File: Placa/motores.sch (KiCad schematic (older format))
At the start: 13 parts, among them P3 CONN_5X2

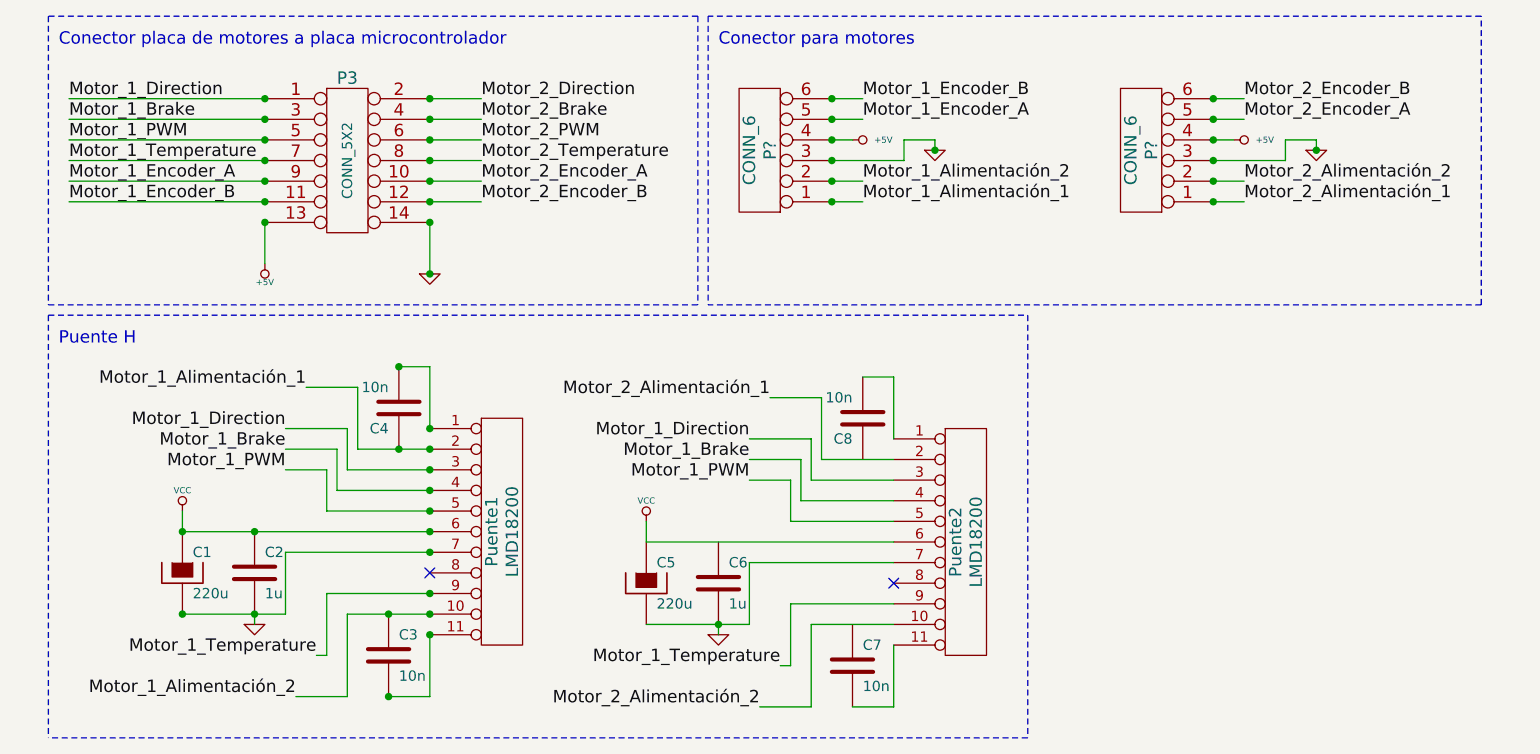
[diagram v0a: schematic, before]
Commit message: Termino PCB motores. Agrego biblioteca LMD18200. Agrego el anteproyecto hecho por Gisela.
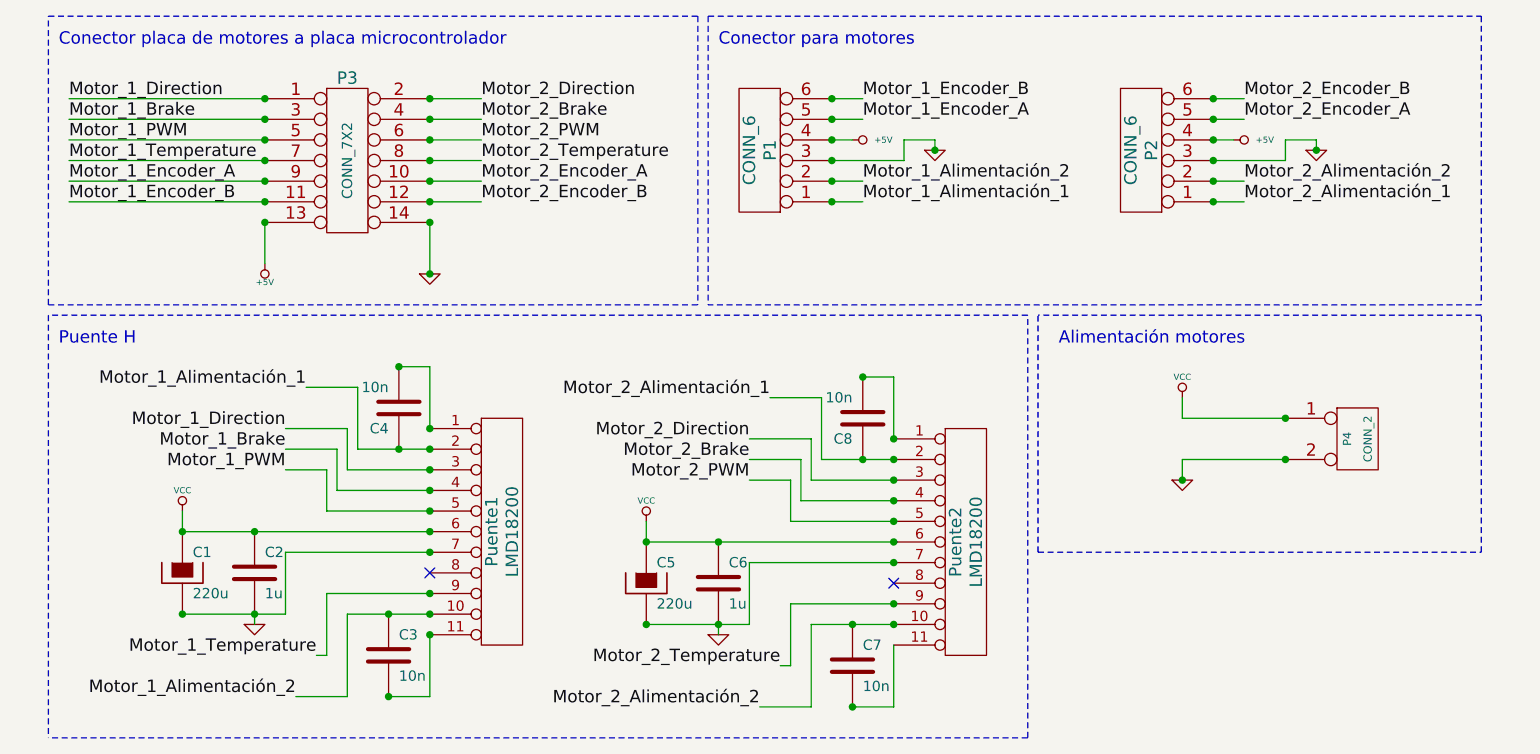
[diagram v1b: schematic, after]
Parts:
- added P4: CONN_2, symbol CONN_2
- P3: value CONN_5X2 -> CONN_7X2
- gave numbers to parts that had none: 2
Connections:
- net GND: now also P4.2 (PM)
- net Motor_1_Brake: no longer Puente2.4 (P4)
- net Motor_1_Direction: no longer Puente2.3 (P3)
- net Motor_1_PWM: no longer Puente2.5 (P5)
- net Motor_1_Temperature: no longer Puente2.9 (P9)
- net Motor_2_Alimentación_1: now also C8.1
- net Motor_2_Alimentación_2: now also C7.1
- net Motor_2_Brake: now also Puente2.4 (P4)
- net Motor_2_Direction: now also Puente2.3 (P3)
- net Motor_2_PWM: now also Puente2.5 (P5)
- net Motor_2_Temperature: now also Puente2.9 (P9)
- net VCC: now also C6.1, P4.1 (P1)
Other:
- note added: "Alimentación motores"

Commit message: Agrego archivos placa potencia. Agrego biblioteca ptn78020w.
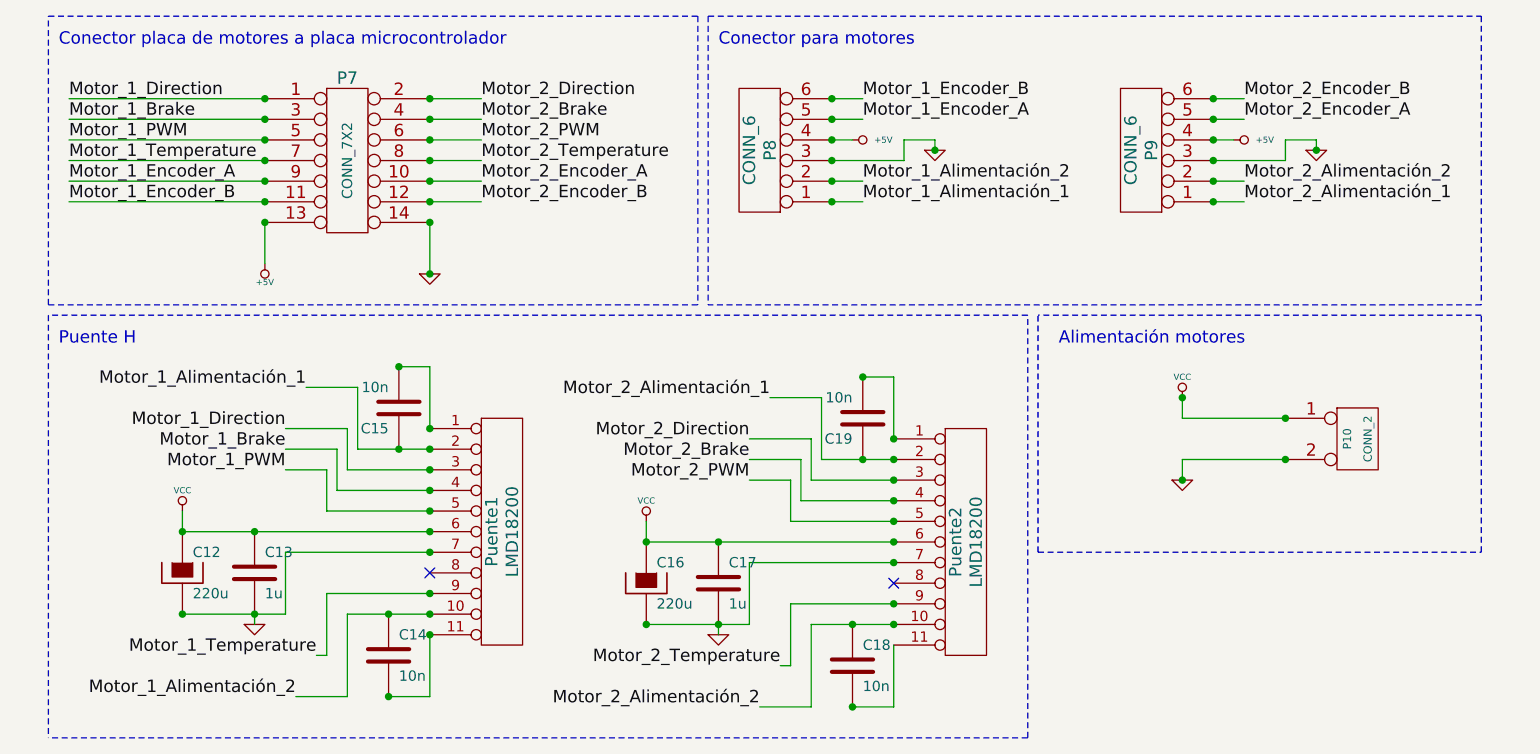
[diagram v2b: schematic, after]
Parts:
- renumbered C1 to C12, C2 to C13, C3 to C14, C4 to C15, C5 to C16, C6 to C17, C7 to C18, C8 to C19, P4 to P10, P3 to P7, P1 to P8, P2 to P9
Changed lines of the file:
@@
-EESchema Schematic File Version 2  date mar 30 abr 2013 20:08:31 ART
+EESchema Schematic File Version 2  date sáb 25 may 2013 16:00:35 ART
 LIBS:power
 LIBS:device
@@
 LIBS:contrib
 LIBS:valves
-LIBS:motores-cache
+LIBS:cny70
+LIBS:L298
+LIBS:ptn4050
+LIBS:ptn78000w
+LIBS:ptn78020w
+LIBS:TCO-cache
 EELAYER 25  0
 EELAYER END
 $Descr A4 11700 8267
 encoding utf-8
-Sheet 1 1
+Sheet 4 5
 Title "TCO - Placa motores"
-Date "30 apr 2013"
+Date "25 may 2013"
 Rev "1"
 Comp ""
@@
 Comment4 ""
 $EndDescr
+Connection ~ 6000 2350
 Connection ~ 6000 2750
 Connection ~ 6500 2450
 Connection ~ 6500 2650
 $Comp
-L GND #PWR01
+L GND #PWR035
 U 1 1 5180451D
 P 6000 2750
-F 0 "#PWR01" H 6000 2750 30  0001 C CNN
+F 0 "#PWR035" H 6000 2750 30  0001 C CNN
 F 1 "GND" H 6000 2680 30  0001 C CNN
 	1    6000 2750
@@
 $EndComp
 $Comp
-L VCC #PWR02
+L VCC #PWR036
 U 1 1 51804519
 P 6000 2350
-F 0 "#PWR02" H 6000 2450 30  0001 C CNN
+F 0 "#PWR036" H 6000 2450 30  0001 C CNN
 F 1 "VCC" H 6000 2450 30  0000 C CNN
 	1    6000 2350
@@
 	6000 2450 6000 2350
 $Comp
-L CONN_2 P4
+L CONN_2 P10
 U 1 1 5180450D
 P 6850 2550
-F 0 "P4" V 6800 2550 40  0000 C CNN
+F 0 "P10" V 6800 2550 40  0000 C CNN
 F 1 "CONN_2" V 6900 2550 40  0000 C CNN
 	1    6850 2550
@@
 Puente H
 $Comp
-L CONN_6 P2
+L CONN_6 P9
 U 1 1 517D87F6
 P 5800 1150
-F 0 "P2" V 5750 1150 60  0000 C CNN
+F 0 "P9" V 5750 1150 60  0000 C CNN
 F 1 "CONN_6" V 5850 1150 60  0000 C CNN
 	1    5800 1150
@@
 Motor_2_Alimentación_2
 $Comp
-L +5V #PWR03
+L +5V #PWR037
 U 1 1 517D87F5
 P 6250 1100
-F 0 "#PWR03" H 6250 1190 20  0001 C CNN
+F 0 "#PWR037" H 6250 1190 20  0001 C CNN
 F 1 "+5V" V 6250 1250 30  0000 C CNN
 	1    6250 1100
@@
 $EndComp
 $Comp
-L GND #PWR04
+L GND #PWR038
 U 1 1 517D87F4
 P 6650 1150
-F 0 "#PWR04" H 6650 1150 30  0001 C CNN
+F 0 "#PWR038" H 6650 1150 30  0001 C CNN
 F 1 "GND" H 6650 1080 30  0001 C CNN
 	1    6650 1150
@@
 Motor_1_Encoder_A
 $Comp
-L GND #PWR05
+L GND #PWR039
 U 1 1 517D878E
 P 4800 1150
-F 0 "#PWR05" H 4800 1150 30  0001 C CNN
+F 0 "#PWR039" H 4800 1150 30  0001 C CNN
 F 1 "GND" H 4800 1080 30  0001 C CNN
 	1    4800 1150
@@
 $EndComp
 $Comp
-L +5V #PWR06
+L +5V #PWR040
 U 1 1 517D877F
 P 4400 1100
-F 0 "#PWR06" H 4400 1190 20  0001 C CNN
+F 0 "#PWR040" H 4400 1190 20  0001 C CNN
 F 1 "+5V" V 4400 1250 30  0000 C CNN
 	1    4400 1100
@@
 Motor_1_Alimentación_1
 $Comp
-L CONN_6 P1
+L CONN_6 P8
 U 1 1 517D8704
 P 3950 1150
-F 0 "P1" V 3900 1150 60  0000 C CNN
+F 0 "P8" V 3900 1150 60  0000 C CNN
 F 1 "CONN_6" V 4000 1150 60  0000 C CNN
 	1    3950 1150
@@
 Motor_2_Direction
 $Comp
-L C C7
+L C C18
 U 1 1 51769D40
 P 4400 3650
-F 0 "C7" H 4450 3750 50  0000 L CNN
+F 0 "C18" H 4450 3750 50  0000 L CNN
 F 1 "10n" H 4450 3550 50  0000 L CNN
 	1    4400 3650
@@
 NoConn ~ 4600 3250
 $Comp
-L GND #PWR07
+L GND #PWR041
 U 1 1 51769D3F
 P 3750 3500
-F 0 "#PWR07" H 3750 3500 30  0001 C CNN
+F 0 "#PWR041" H 3750 3500 30  0001 C CNN
 F 1 "GND" H 3750 3430 30  0001 C CNN
 	1    3750 3500
@@
 $EndComp
 $Comp
-L C C6
+L C C17
 U 1 1 51769D3E
 P 3750 3250
-F 0 "C6" H 3800 3350 50  0000 L CNN
+F 0 "C17" H 3800 3350 50  0000 L CNN
 F 1 "1u" H 3800 3150 50  0000 L CNN
 	1    3750 3250
@@
 $EndComp
 $Comp
-L CAPAPOL C5
+L CAPAPOL C16
 U 1 1 51769D3D
 P 3400 3250
-F 0 "C5" H 3450 3350 50  0000 L CNN
+F 0 "C16" H 3450 3350 50  0000 L CNN
 F 1 "220u" H 3450 3150 50  0000 L CNN
 	1    3400 3250
@@
 $EndComp
 $Comp
-L VCC #PWR08
+L VCC #PWR042
 U 1 1 51769D3C
 P 3400 2950
-F 0 "#PWR08" H 3400 3050 30  0001 C CNN
+F 0 "#PWR042" H 3400 3050 30  0001 C CNN
 F 1 "VCC" H 3400 3050 30  0000 C CNN
 	1    3400 2950
@@
 $EndComp
 $Comp
-L C C8
+L C C19
 U 1 1 51769D3B
 P 4450 2450
-F 0 "C8" H 4500 2550 50  0000 L CNN
+F 0 "C19" H 4500 2550 50  0000 L CNN
 F 1 "10n" H 4500 2350 50  0000 L CNN
 	1    4450 2450
@@
 Motor_1_Direction
 $Comp
-L GND #PWR09
+L GND #PWR043
 U 1 1 51755C0C
 P 2350 1750
-F 0 "#PWR09" H 2350 1750 30  0001 C CNN
+F 0 "#PWR043" H 2350 1750 30  0001 C CNN
 F 1 "GND" H 2350 1680 30  0001 C CNN
 	1    2350 1750
@@
 $EndComp
 $Comp
-L +5V #PWR010
+L +5V #PWR044
 U 1 1 51755BFF
 P 1550 1700
-F 0 "#PWR010" H 1550 1790 20  0001 C CNN
+F 0 "#PWR044" H 1550 1790 20  0001 C CNN
 F 1 "+5V" H 1550 1790 30  0000 C CNN
 	1    1550 1700
@@
 Motor_1_Direction
 $Comp
-L CONN_7X2 P3
+L CONN_7X2 P7
 U 1 1 517556DB
 P 1950 1200
-F 0 "P3" H 1950 1600 60  0000 C CNN
+F 0 "P7" H 1950 1600 60  0000 C CNN
 F 1 "CONN_7X2" V 1950 1200 50  0000 C CNN
 	1    1950 1200
@@
 $EndComp
 $Comp
-L C C3
+L C C14
 U 1 1 51755634
 P 2150 3600
-F 0 "C3" H 2200 3700 50  0000 L CNN
+F 0 "C14" H 2200 3700 50  0000 L CNN
 F 1 "10n" H 2200 3500 50  0000 L CNN
 	1    2150 3600
@@
 NoConn ~ 2350 3200
 $Comp
-L GND #PWR011
+L GND #PWR045
 U 1 1 5175560C
 P 1500 3450
-F 0 "#PWR011" H 1500 3450 30  0001 C CNN
+F 0 "#PWR045" H 1500 3450 30  0001 C CNN
 F 1 "GND" H 1500 3380 30  0001 C CNN
 	1    1500 3450
@@
 $EndComp
 $Comp
-L C C2
+L C C13
 U 1 1 517555EE
 P 1500 3200
-F 0 "C2" H 1550 3300 50  0000 L CNN
+F 0 "C13" H 1550 3300 50  0000 L CNN
 F 1 "1u" H 1550 3100 50  0000 L CNN
 	1    1500 3200
@@
 $EndComp
 $Comp
-L CAPAPOL C1
+L CAPAPOL C12
 U 1 1 517555DF
 P 1150 3200
-F 0 "C1" H 1200 3300 50  0000 L CNN
+F 0 "C12" H 1200 3300 50  0000 L CNN
 F 1 "220u" H 1200 3100 50  0000 L CNN
 	1    1150 3200
@@
 $EndComp
 $Comp
-L VCC #PWR012
+L VCC #PWR046
 U 1 1 517555C8
 P 1150 2900
-F 0 "#PWR012" H 1150 3000 30  0001 C CNN
+F 0 "#PWR046" H 1150 3000 30  0001 C CNN
 F 1 "VCC" H 1150 3000 30  0000 C CNN
 	1    1150 2900
@@
 $EndComp
 $Comp
-L C C4
+L C C15
 U 1 1 5175549B
 P 2200 2400
-F 0 "C4" H 2250 2500 50  0000 L CNN
+F 0 "C15" H 2250 2500 50  0000 L CNN
 F 1 "10n" H 2250 2300 50  0000 L CNN
 	1    2200 2400

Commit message: Agrego retoques en 2da revisión PCB micro
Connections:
- net labels added: +12V
- net labels removed: VCC
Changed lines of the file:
@@
-EESchema Schematic File Version 2  date mar 11 jun 2013 16:06:38 ART
+EESchema Schematic File Version 2  date mar 11 jun 2013 16:28:51 ART
 LIBS:power
 LIBS:device
@@
 Comment4 ""
 $EndDescr
+$Comp
+L +12V #PWR032
+U 1 1 51B77652
+P 1150 2900
+F 0 "#PWR032" H 1150 2850 20  0001 C CNN
+F 1 "+12V" H 1150 3000 30  0000 C CNN
+	1    1150 2900
+	1    0    0    -1
+$EndComp
+$Comp
+L +12V #PWR033
+U 1 1 51B7764D
+P 3400 2950
+F 0 "#PWR033" H 3400 2900 20  0001 C CNN
+F 1 "+12V" H 3400 3050 30  0000 C CNN
+	1    3400 2950
+	1    0    0    -1
+$EndComp
+$Comp
+L +12V #PWR034
+U 1 1 51B77648
+P 6000 2350
+F 0 "#PWR034" H 6000 2300 20  0001 C CNN
+F 1 "+12V" H 6000 2450 30  0000 C CNN
+	1    6000 2350
+	1    0    0    -1
+$EndComp
 Connection ~ 6000 2350
 Connection ~ 6000 2750
@@
 Connection ~ 6500 2650
 $Comp
-L GND #PWR44
+L GND #PWR035
 U 1 1 5180451D
 P 6000 2750
-F 0 "#PWR44" H 6000 2750 30  0001 C CNN
+F 0 "#PWR035" H 6000 2750 30  0001 C CNN
 F 1 "GND" H 6000 2680 30  0001 C CNN
 	1    6000 2750
-	1    0    0    -1
-$EndComp
-$Comp
-L VCC #PWR43
-U 1 1 51804519
-P 6000 2350
-F 0 "#PWR43" H 6000 2450 30  0001 C CNN
-F 1 "VCC" H 6000 2450 30  0000 C CNN
-	1    6000 2350
 	1    0    0    -1
 $EndComp
@@
 Motor_2_Alimentación_2
 $Comp
-L +5V #PWR45
+L +5V #PWR036
 U 1 1 517D87F5
 P 6250 1100
-F 0 "#PWR45" H 6250 1190 20  0001 C CNN
+F 0 "#PWR036" H 6250 1190 20  0001 C CNN
 F 1 "+5V" V 6250 1250 30  0000 C CNN
 	1    6250 1100
@@
 $EndComp
 $Comp
-L GND #PWR46
+L GND #PWR037
 U 1 1 517D87F4
 P 6650 1150
-F 0 "#PWR46" H 6650 1150 30  0001 C CNN
+F 0 "#PWR037" H 6650 1150 30  0001 C CNN
 F 1 "GND" H 6650 1080 30  0001 C CNN
 	1    6650 1150
@@
 Motor_1_Encoder_A
 $Comp
-L GND #PWR42
+L GND #PWR038
 U 1 1 517D878E
 P 4800 1150
-F 0 "#PWR42" H 4800 1150 30  0001 C CNN
+F 0 "#PWR038" H 4800 1150 30  0001 C CNN
 F 1 "GND" H 4800 1080 30  0001 C CNN
 	1    4800 1150
@@
 $EndComp
 $Comp
-L +5V #PWR41
+L +5V #PWR039
 U 1 1 517D877F
 P 4400 1100
-F 0 "#PWR41" H 4400 1190 20  0001 C CNN
+F 0 "#PWR039" H 4400 1190 20  0001 C CNN
 F 1 "+5V" V 4400 1250 30  0000 C CNN
 	1    4400 1100
@@
 NoConn ~ 4600 3250
 $Comp
-L GND #PWR40
+L GND #PWR040
 U 1 1 51769D3F
 P 3750 3500
-F 0 "#PWR40" H 3750 3500 30  0001 C CNN
+F 0 "#PWR040" H 3750 3500 30  0001 C CNN
 F 1 "GND" H 3750 3430 30  0001 C CNN
 	1    3750 3500
@@
 F 1 "220u" H 3450 3150 50  0000 L CNN
 	1    3400 3250
-	1    0    0    -1
-$EndComp
-$Comp
-L VCC #PWR39
-U 1 1 51769D3C
-P 3400 2950
-F 0 "#PWR39" H 3400 3050 30  0001 C CNN
-F 1 "VCC" H 3400 3050 30  0000 C CNN
-	1    3400 2950
 	1    0    0    -1
 $EndComp
@@
 Motor_1_Direction
 $Comp
-L GND #PWR38
+L GND #PWR041
 U 1 1 51755C0C
 P 2350 1750
-F 0 "#PWR38" H 2350 1750 30  0001 C CNN
+F 0 "#PWR041" H 2350 1750 30  0001 C CNN
 F 1 "GND" H 2350 1680 30  0001 C CNN
 	1    2350 1750
@@
 $EndComp
 $Comp
-L +5V #PWR37
+L +5V #PWR042
 U 1 1 51755BFF
 P 1550 1700
-F 0 "#PWR37" H 1550 1790 20  0001 C CNN
+F 0 "#PWR042" H 1550 1790 20  0001 C CNN
 F 1 "+5V" H 1550 1790 30  0000 C CNN
 	1    1550 1700
@@
 NoConn ~ 2350 3200
 $Comp
-L GND #PWR36
+L GND #PWR043
 U 1 1 5175560C
 P 1500 3450
-F 0 "#PWR36" H 1500 3450 30  0001 C CNN
+F 0 "#PWR043" H 1500 3450 30  0001 C CNN
 F 1 "GND" H 1500 3380 30  0001 C CNN
 	1    1500 3450
@@
 	1    0    0    -1
 $EndComp
-$Comp
-L VCC #PWR35
-U 1 1 517555C8
-P 1150 2900
-F 0 "#PWR35" H 1150 3000 30  0001 C CNN
-F 1 "VCC" H 1150 3000 30  0000 C CNN
-	1    1150 2900
-	1    0    0    -1
-$EndComp

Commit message: Agrego medición del piso, pero no funciona. Seguramente olvidé alguna configuración.
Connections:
- net labels added: VCC
- net labels removed: +12V
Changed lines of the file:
@@
-EESchema Schematic File Version 2  date mar 11 jun 2013 16:28:51 ART
+EESchema Schematic File Version 2  date jue 06 jun 2013 20:07:57 ART
 LIBS:power
 LIBS:device
@@
 LIBS:ptn78000w
 LIBS:ptn78020w
-LIBS:TCO-cache
 EELAYER 25  0
 EELAYER END
@@
 Sheet 4 5
 Title "TCO - Placa motores"
-Date "11 jun 2013"
-Rev "2"
+Date "6 jun 2013"
+Rev "1"
 Comp ""
 Comment1 ""
@@
 Comment4 ""
 $EndDescr
-$Comp
-L +12V #PWR032
-U 1 1 51B77652
-P 1150 2900
-F 0 "#PWR032" H 1150 2850 20  0001 C CNN
-F 1 "+12V" H 1150 3000 30  0000 C CNN
-	1    1150 2900
-	1    0    0    -1
-$EndComp
-$Comp
-L +12V #PWR033
-U 1 1 51B7764D
-P 3400 2950
-F 0 "#PWR033" H 3400 2900 20  0001 C CNN
-F 1 "+12V" H 3400 3050 30  0000 C CNN
-	1    3400 2950
-	1    0    0    -1
-$EndComp
-$Comp
-L +12V #PWR034
-U 1 1 51B77648
-P 6000 2350
-F 0 "#PWR034" H 6000 2300 20  0001 C CNN
-F 1 "+12V" H 6000 2450 30  0000 C CNN
-	1    6000 2350
-	1    0    0    -1
-$EndComp
 Connection ~ 6000 2350
 Connection ~ 6000 2750
@@
 Connection ~ 6500 2650
 $Comp
-L GND #PWR035
+L GND #PWR44
 U 1 1 5180451D
 P 6000 2750
-F 0 "#PWR035" H 6000 2750 30  0001 C CNN
+F 0 "#PWR44" H 6000 2750 30  0001 C CNN
 F 1 "GND" H 6000 2680 30  0001 C CNN
 	1    6000 2750
+	1    0    0    -1
+$EndComp
+$Comp
+L VCC #PWR43
+U 1 1 51804519
+P 6000 2350
+F 0 "#PWR43" H 6000 2450 30  0001 C CNN
+F 1 "VCC" H 6000 2450 30  0000 C CNN
+	1    6000 2350
 	1    0    0    -1
 $EndComp
@@
 Motor_2_Alimentación_2
 $Comp
-L +5V #PWR036
+L +5V #PWR45
 U 1 1 517D87F5
 P 6250 1100
-F 0 "#PWR036" H 6250 1190 20  0001 C CNN
+F 0 "#PWR45" H 6250 1190 20  0001 C CNN
 F 1 "+5V" V 6250 1250 30  0000 C CNN
 	1    6250 1100
@@
 $EndComp
 $Comp
-L GND #PWR037
+L GND #PWR46
 U 1 1 517D87F4
 P 6650 1150
-F 0 "#PWR037" H 6650 1150 30  0001 C CNN
+F 0 "#PWR46" H 6650 1150 30  0001 C CNN
 F 1 "GND" H 6650 1080 30  0001 C CNN
 	1    6650 1150
@@
 Motor_1_Encoder_A
 $Comp
-L GND #PWR038
+L GND #PWR42
 U 1 1 517D878E
 P 4800 1150
-F 0 "#PWR038" H 4800 1150 30  0001 C CNN
+F 0 "#PWR42" H 4800 1150 30  0001 C CNN
 F 1 "GND" H 4800 1080 30  0001 C CNN
 	1    4800 1150
@@
 $EndComp
 $Comp
-L +5V #PWR039
+L +5V #PWR41
 U 1 1 517D877F
 P 4400 1100
-F 0 "#PWR039" H 4400 1190 20  0001 C CNN
+F 0 "#PWR41" H 4400 1190 20  0001 C CNN
 F 1 "+5V" V 4400 1250 30  0000 C CNN
 	1    4400 1100
@@
 NoConn ~ 4600 3250
 $Comp
-L GND #PWR040
+L GND #PWR40
 U 1 1 51769D3F
 P 3750 3500
-F 0 "#PWR040" H 3750 3500 30  0001 C CNN
+F 0 "#PWR40" H 3750 3500 30  0001 C CNN
 F 1 "GND" H 3750 3430 30  0001 C CNN
 	1    3750 3500
@@
 F 1 "220u" H 3450 3150 50  0000 L CNN
 	1    3400 3250
+	1    0    0    -1
+$EndComp
+$Comp
+L VCC #PWR39
+U 1 1 51769D3C
+P 3400 2950
+F 0 "#PWR39" H 3400 3050 30  0001 C CNN
+F 1 "VCC" H 3400 3050 30  0000 C CNN
+	1    3400 2950
 	1    0    0    -1
 $EndComp
@@
 Motor_1_Direction
 $Comp
-L GND #PWR041
+L GND #PWR38
 U 1 1 51755C0C
 P 2350 1750
-F 0 "#PWR041" H 2350 1750 30  0001 C CNN
+F 0 "#PWR38" H 2350 1750 30  0001 C CNN
 F 1 "GND" H 2350 1680 30  0001 C CNN
 	1    2350 1750
@@
 $EndComp
 $Comp
-L +5V #PWR042
+L +5V #PWR37
 U 1 1 51755BFF
 P 1550 1700
-F 0 "#PWR042" H 1550 1790 20  0001 C CNN
+F 0 "#PWR37" H 1550 1790 20  0001 C CNN
 F 1 "+5V" H 1550 1790 30  0000 C CNN
 	1    1550 1700
@@
 NoConn ~ 2350 3200
 $Comp
-L GND #PWR043
+L GND #PWR36
 U 1 1 5175560C
 P 1500 3450
-F 0 "#PWR043" H 1500 3450 30  0001 C CNN
+F 0 "#PWR36" H 1500 3450 30  0001 C CNN
 F 1 "GND" H 1500 3380 30  0001 C CNN
 	1    1500 3450
@@
 	1    0    0    -1
 $EndComp
+$Comp
+L VCC #PWR35
+U 1 1 517555C8
+P 1150 2900
+F 0 "#PWR35" H 1150 3000 30  0001 C CNN
+F 1 "VCC" H 1150 3000 30  0000 C CNN
+	1    1150 2900
+	1    0    0    -1
+$EndComp
